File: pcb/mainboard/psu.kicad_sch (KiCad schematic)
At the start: 128 parts, among them J1 CONN_PCIE_PWR_8PIN, J2 CONN_IBC_MGMT, J3 CONN_01X03, J4 CONN_01X05, SW1 SWITCH, SW2 SWITCH, U1 STM32L031C6U6, U2 MYMGK1R812ERSR, U26 LMR70503, U3 MYMGK00504ERSR, U37 ZLDO1117x50TA, U4 MYMGK00504ERSR, U5 MYMGK00504ERSR, U6 MYMGK00504ERSR, U7 MYMGK00504ERSR

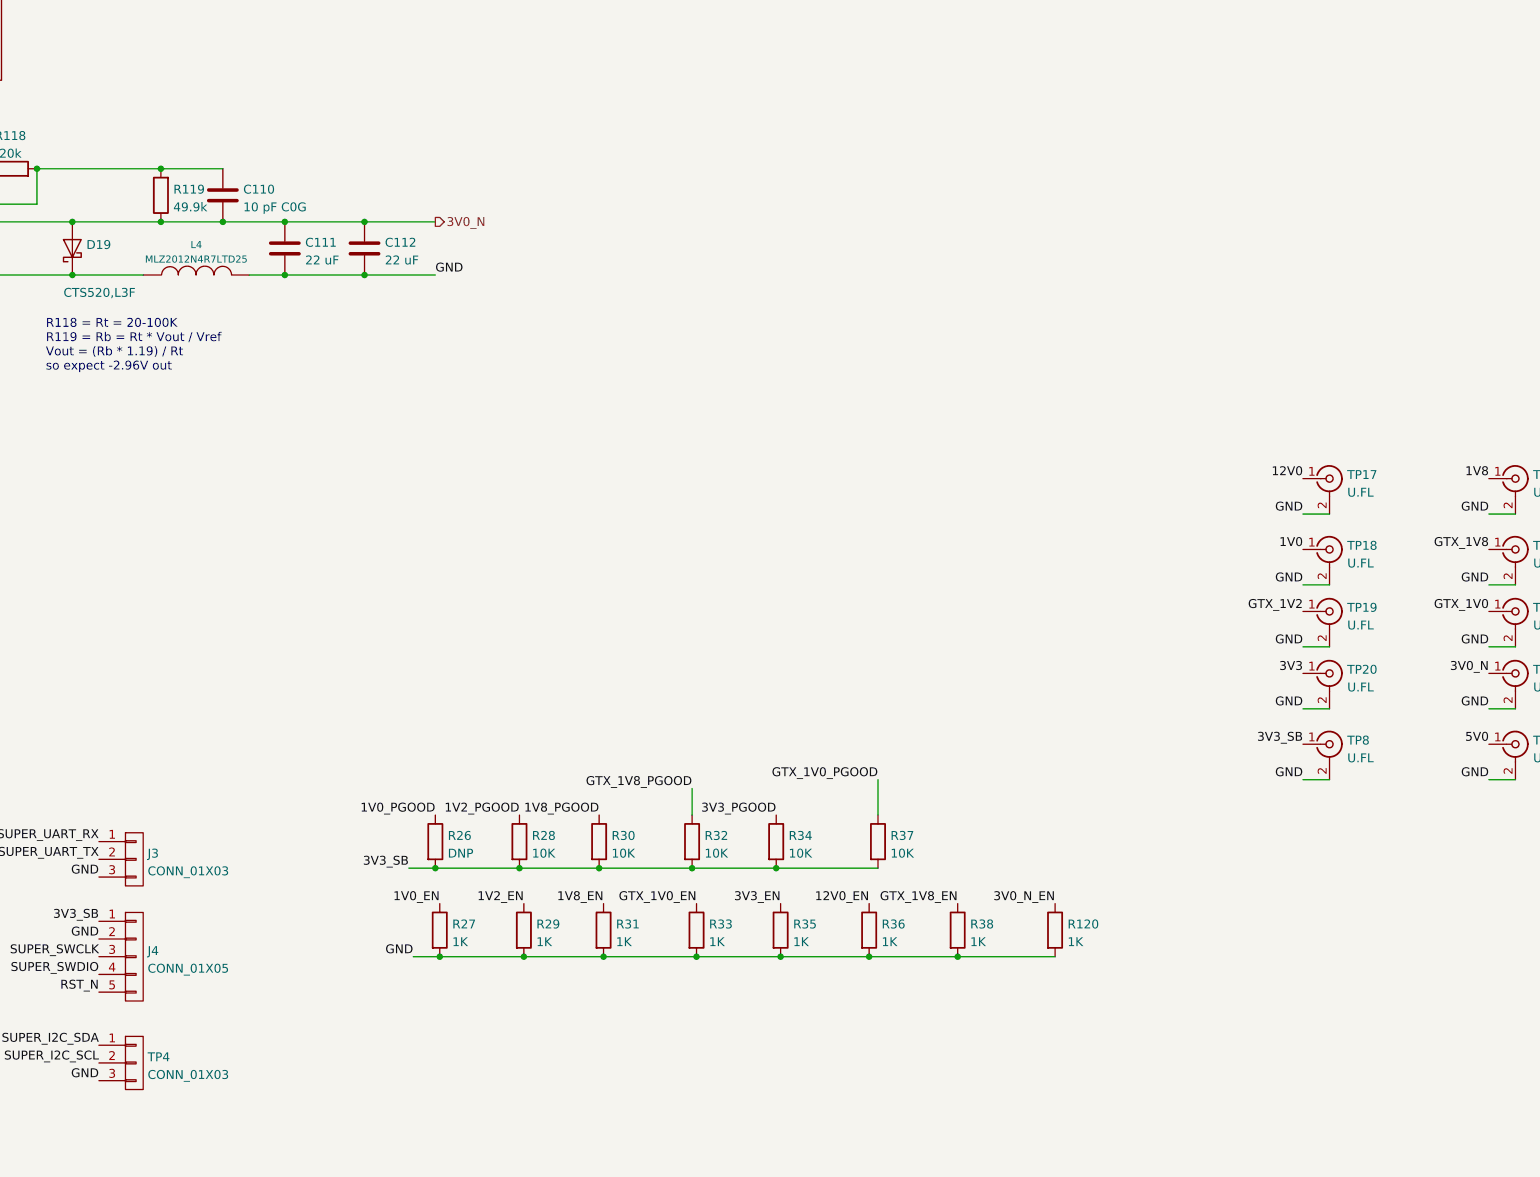
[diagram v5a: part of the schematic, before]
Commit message: Finished initial schematic review of trigger crossbar mainboard
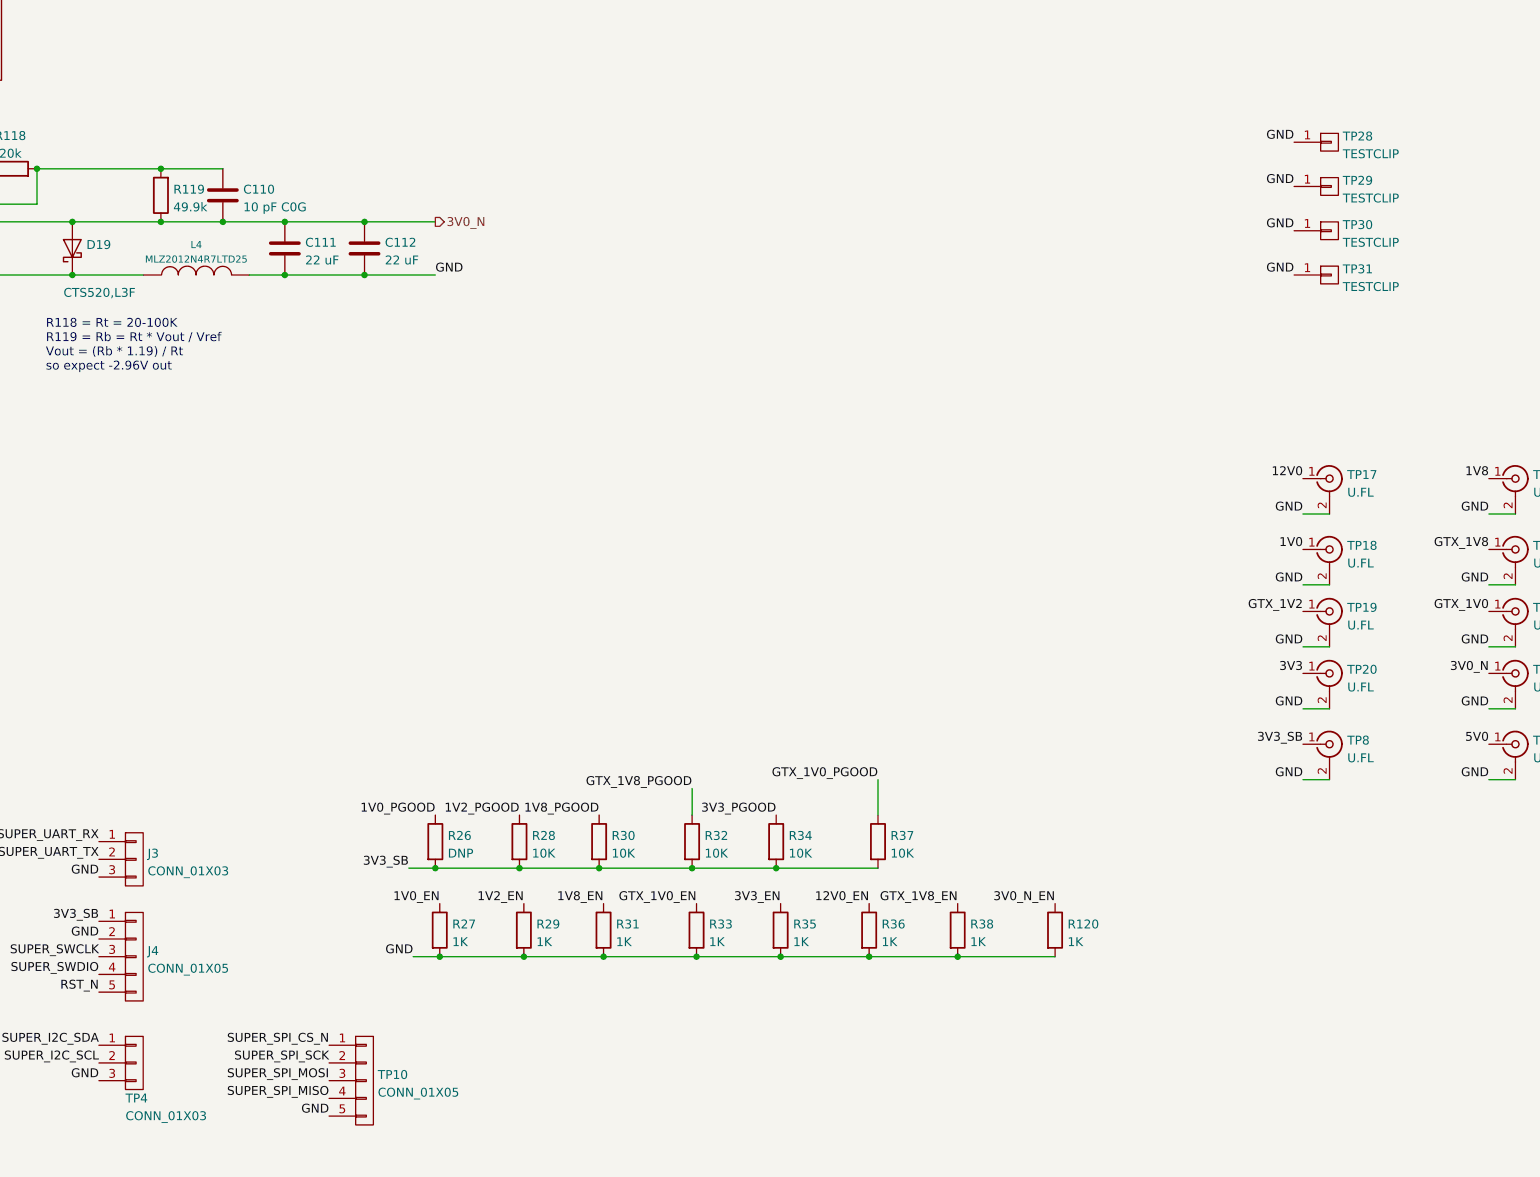
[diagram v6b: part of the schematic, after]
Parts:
- added TP10: CONN_01X05, azonenberg_pcb:CONN_HEADER_2.54MM_1x5, symbol conn:CONN_01X05
- added TP28, TP29, TP30, TP31: TESTCLIP, azonenberg_pcb:TESTPOINT_SMT_KEYSTONE_5016, symbol conn:CONN_01X01
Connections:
- net GND: now also TP10.5 (P5), TP28.1 (P1), TP29.1 (P1), TP30.1 (P1), TP31.1 (P1)
- net SUPER_SPI_CS_N: now also TP10.1 (P1)
- net SUPER_SPI_MISO: now also TP10.4 (P4)
- net SUPER_SPI_MOSI: now also TP10.3 (P3)
- net SUPER_SPI_SCK: now also TP10.2 (P2)
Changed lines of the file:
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@@
   (title_block
     (title "Trigger Crossbar")
-    (date "2023-12-18")
+    (date "2023-12-19")
     (rev "0.1")
     (company "Antikernel Labs")
@@
     (effects (font (size 1.27 1.27)) (justify left bottom))
   )
+  (label "SUPER_SPI_CS_N" (at 309.88 384.81 180)
+    (effects (font (size 1.27 1.27)) (justify right bottom))
+  )
   (label "3V3_SB" (at 110.49 350.52 180)
     (effects (font (size 1.27 1.27)) (justify right bottom))
@@
     (effects (font (size 1.27 1.27)) (justify right bottom))
   )
+  (label "SUPER_SPI_SCK" (at 309.88 387.35 180)
+    (effects (font (size 1.27 1.27)) (justify right bottom))
+  )
   (label "RST_N" (at 217.17 383.54 180)
     (effects (font (size 1.27 1.27)) (justify right bottom))
@@
     (effects (font (size 1.27 1.27)) (justify right bottom))
   )
+  (label "GND" (at 448.31 261.62 180)
+    (effects (font (size 1.27 1.27)) (justify right bottom))
+  )
   (label "1V0_PGOOD" (at 78.74 358.14 180)
     (effects (font (size 1.27 1.27)) (justify right bottom))
@@
     (effects (font (size 1.27 1.27)) (justify right bottom))
   )
+  (label "SUPER_SPI_MISO" (at 309.88 392.43 180)
+    (effects (font (size 1.27 1.27)) (justify right bottom))
+  )
   (label "3V3_SB" (at 217.17 367.03 180)
     (effects (font (size 1.27 1.27)) (justify right bottom))
@@
     (effects (font (size 1.27 1.27)) (justify left bottom))
   )
+  (label "GND" (at 448.31 255.27 180)
+    (effects (font (size 1.27 1.27)) (justify right bottom))
+  )
   (label "GTX_1V8" (at 265.43 139.7 0)
     (effects (font (size 1.27 1.27)) (justify left bottom))
@@
     (effects (font (size 1.27 1.27)) (justify right bottom))
   )
+  (label "GND" (at 309.88 394.97 180)
+    (effects (font (size 1.27 1.27)) (justify right bottom))
+  )
   (label "GTX_1V0_EN" (at 78.74 375.92 180)
     (effects (font (size 1.27 1.27)) (justify right bottom))
@@
     (effects (font (size 1.27 1.27)) (justify right bottom))
   )
+  (label "GND" (at 448.31 267.97 180)
+    (effects (font (size 1.27 1.27)) (justify right bottom))
+  )
+  (label "SUPER_SPI_MOSI" (at 309.88 389.89 180)
+    (effects (font (size 1.27 1.27)) (justify right bottom))
+  )
   (label "A3V3_SUPER" (at 245.11 355.6 0)
     (effects (font (size 1.27 1.27)) (justify left bottom))
@@
     (effects (font (size 1.27 1.27)) (justify right bottom))
   )
+  (label "GND" (at 448.31 274.32 180)
+    (effects (font (size 1.27 1.27)) (justify right bottom))
+  )
   (label "12V0_EN" (at 41.91 63.5 0)
     (effects (font (size 1.27 1.27)) (justify left bottom))
@@
   )
   (symbol (lib_id "conn:CONN_01X03") (at 281.94 387.35 0) (unit 1)
-    (in_bom yes) (on_board yes) (fields_autoplaced)
-    (property "Reference" "TP4" (id 0) (at 283.845 386.5153 0)
+    (in_bom yes) (on_board yes)
+    (property "Reference" "TP4" (id 0) (at 280.67 392.43 0)
       (effects (font (size 1.27 1.27)) (justify left))
     )
-    (property "Value" "CONN_01X03" (id 1) (at 283.845 389.0522 0)
+    (property "Value" "CONN_01X03" (id 1) (at 280.67 394.9669 0)
       (effects (font (size 1.27 1.27)) (justify left))
     )
@@
     (pin "2")
   )
+  (symbol (lib_id "conn:CONN_01X01") (at 453.39 255.27 0) (unit 1)
+    (in_bom yes) (on_board yes) (fields_autoplaced)
+    (property "Reference" "TP28" (id 0) (at 455.295 254.4353 0)
+      (effects (font (size 1.27 1.27)) (justify left))
+    )
+    (property "Value" "TESTCLIP" (id 1) (at 455.295 256.9722 0)
+      (effects (font (size 1.27 1.27)) (justify left))
+    )
+    (property "Footprint" "azonenberg_pcb:TESTPOINT_SMT_KEYSTONE_5016" (id 2) (at 453.39 255.27 0)
+      (effects (font (size 1.27 1.27)) hide)
+    )
+    (property "Datasheet" "" (id 3) (at 453.39 255.27 0)
+      (effects (font (size 1.27 1.27)) hide)
+    )
+    (pin "1")
+  )
   (symbol (lib_id "passive-azonenberg:INDUCTOR_PWROUT") (at 231.14 355.6 270) (unit 1)
     (in_bom yes) (on_board yes) (fields_autoplaced)
@@
     (pin "2")
   )
+  (symbol (lib_id "conn:CONN_01X01") (at 453.39 261.62 0) (unit 1)
+    (in_bom yes) (on_board yes) (fields_autoplaced)
+    (property "Reference" "TP29" (id 0) (at 455.295 260.7853 0)
+      (effects (font (size 1.27 1.27)) (justify left))
+    )
+    (property "Value" "TESTCLIP" (id 1) (at 455.295 263.3222 0)
+      (effects (font (size 1.27 1.27)) (justify left))
+    )
+    (property "Footprint" "azonenberg_pcb:TESTPOINT_SMT_KEYSTONE_5016" (id 2) (at 453.39 261.62 0)
+      (effects (font (size 1.27 1.27)) hide)
+    )
+    (property "Datasheet" "" (id 3) (at 453.39 261.62 0)
+      (effects (font (size 1.27 1.27)) hide)
+    )
+    (pin "1")
+  )
   (symbol (lib_id "device:R") (at 400.05 368.3 0) (unit 1)
     (in_bom yes) (on_board yes) (fields_autoplaced)
@@
     (pin "2")
   )
+  (symbol (lib_id "conn:CONN_01X05") (at 314.96 389.89 0) (unit 1)
+    (in_bom yes) (on_board yes) (fields_autoplaced)
+    (property "Reference" "TP10" (id 0) (at 316.865 389.0553 0)
+      (effects (font (size 1.27 1.27)) (justify left))
+    )
+    (property "Value" "CONN_01X05" (id 1) (at 316.865 391.5922 0)
+      (effects (font (size 1.27 1.27)) (justify left))
+    )
+    (property "Footprint" "azonenberg_pcb:CONN_HEADER_2.54MM_1x5" (id 2) (at 314.96 389.89 0)
+      (effects (font (size 1.27 1.27)) hide)
+    )
+    (property "Datasheet" "" (id 3) (at 314.96 389.89 0)
+      (effects (font (size 1.27 1.27)) hide)
+    )
+    (pin "1")
+    (pin "2")
+    (pin "3")
+    (pin "4")
+    (pin "5")
+  )
   (symbol (lib_id "device:R") (at 104.14 96.52 270) (unit 1)
     (in_bom yes) (on_board yes)
@@
     (pin "2")
   )
+  (symbol (lib_id "conn:CONN_01X01") (at 453.39 267.97 0) (unit 1)
+    (in_bom yes) (on_board yes) (fields_autoplaced)
+    (property "Reference" "TP30" (id 0) (at 455.295 267.1353 0)
+      (effects (font (size 1.27 1.27)) (justify left))
+    )
+    (property "Value" "TESTCLIP" (id 1) (at 455.295 269.6722 0)
+      (effects (font (size 1.27 1.27)) (justify left))
+    )
+    (property "Footprint" "azonenberg_pcb:TESTPOINT_SMT_KEYSTONE_5016" (id 2) (at 453.39 267.97 0)
+      (effects (font (size 1.27 1.27)) hide)
+    )
+    (property "Datasheet" "" (id 3) (at 453.39 267.97 0)
+      (effects (font (size 1.27 1.27)) hide)
+    )
+    (pin "1")
+  )
   (symbol (lib_id "device:C") (at 40.64 77.47 0) (unit 1)
     (in_bom yes) (on_board yes) (fields_autoplaced)
@@
     (pin "2")
   )
+  (symbol (lib_id "conn:CONN_01X01") (at 453.39 274.32 0) (unit 1)
+    (in_bom yes) (on_board yes) (fields_autoplaced)
+    (property "Reference" "TP31" (id 0) (at 455.295 273.4853 0)
+      (effects (font (size 1.27 1.27)) (justify left))
+    )
+    (property "Value" "TESTCLIP" (id 1) (at 455.295 276.0222 0)
+      (effects (font (size 1.27 1.27)) (justify left))
+    )
+    (property "Footprint" "azonenberg_pcb:TESTPOINT_SMT_KEYSTONE_5016" (id 2) (at 453.39 274.32 0)
+      (effects (font (size 1.27 1.27)) hide)
+    )
+    (property "Datasheet" "" (id 3) (at 453.39 274.32 0)
+      (effects (font (size 1.27 1.27)) hide)
+    )
+    (pin "1")
+  )
   (symbol (lib_id "device:R") (at 349.25 368.3 0) (unit 1)
